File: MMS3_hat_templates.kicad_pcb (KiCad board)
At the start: 4 copper layers, 100 x 50 mm, 54 parts, among them J1 Chainbus in, J2 Chainbus Out, J3 Conn_01x04_Pin, J4 AMASS XT60 Male, J5 AMASS XT60 Female, J8 Conn_01x03_Pin, SW1 SW_DIP_x04, U1 SN74CB3Q3384APW, U2 M24C64, U4 AMS1117, U5 LM2596HVS-ADJRG

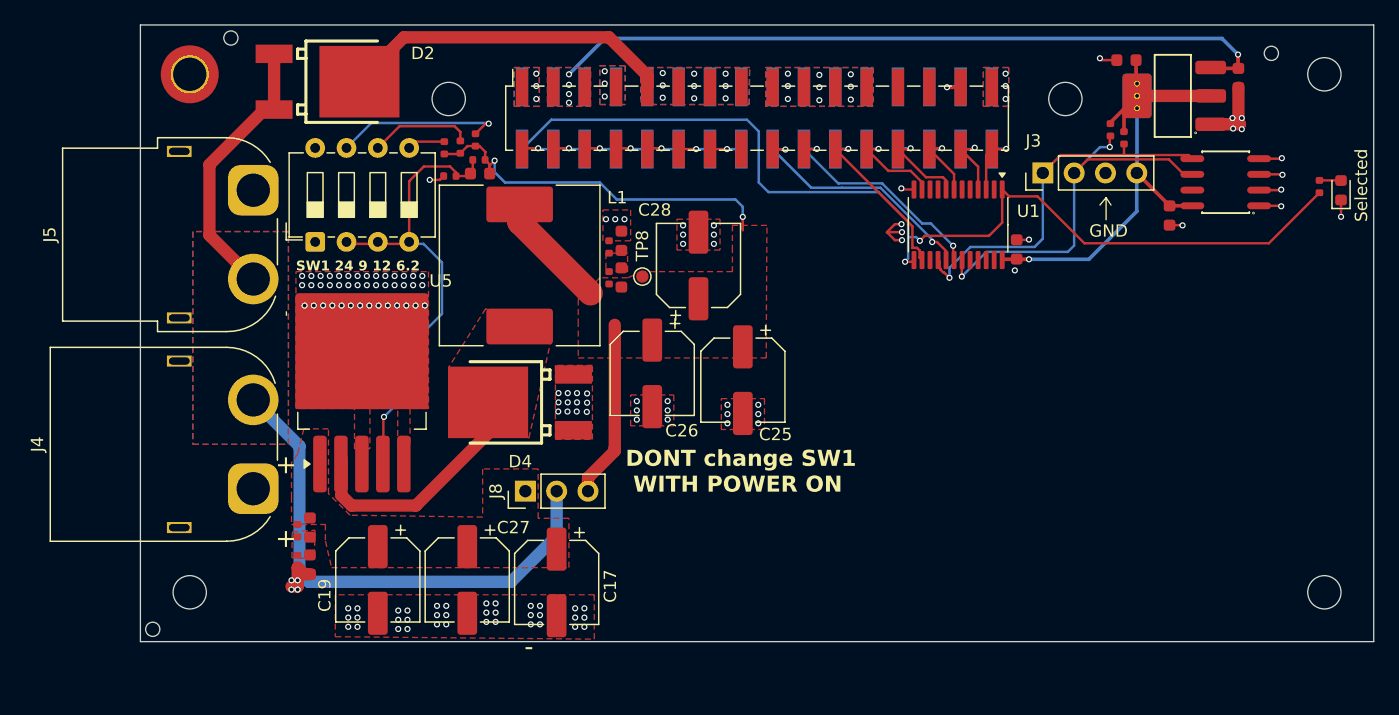
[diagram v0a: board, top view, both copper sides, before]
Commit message: template board cleansed
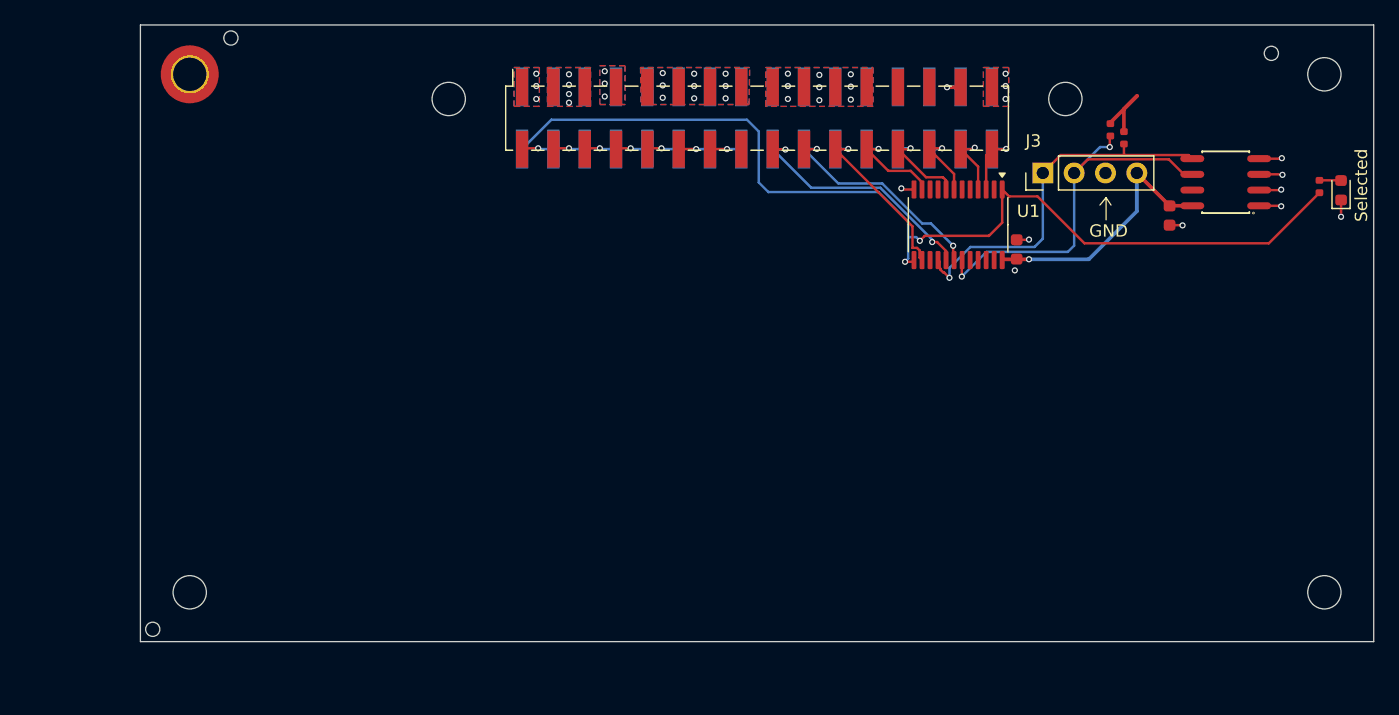
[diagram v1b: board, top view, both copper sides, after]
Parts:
- removed C16, C18: 10uF, PCM_JLCPCB:C_0603
- removed C17, C19, C25, C26, C27, C28: 47u, Capacitor_SMD:CP_Elec_6.3x7.7
- removed C20, C21, C23, C24: 100nF, PCM_JLCPCB:C_0603
- removed C22: 3.3nF, PCM_JLCPCB:C_0603
- removed D2, D4: MBRD10100CTTR, SMC_MBRD10100CTTR:TO-252-3_L6.5-W5.8-P4.58-TL
- removed J4: AMASS XT60 Male, XT60:AMASS_XT60PW-M_1x02_P7.20mm_Horizontal
- removed J5: AMASS XT60 Female, XT60:AMASS_XT60PW-F_1x02_P7.20mm_Horizontal
- removed J8: Conn_01x03_Pin, Connector_PinHeader_2.54mm:PinHeader_1x03_P2.54mm_Vertical
- removed L1: 100uH 4A, Inductor_SMD:L_Sunlord_SWRB1207S
- removed R10, R11, R17, R18: 33kΩ, PCM_JLCPCB:R_0402
- removed R12: 1kΩ, PCM_JLCPCB:R_0402
- removed R13: 18.7k, PCM_JLCPCB:R_0402
- removed R14: 16.5k, PCM_JLCPCB:R_0402
- removed R15: 9.53k, PCM_JLCPCB:R_0402
- removed R16: 5.11k, PCM_JLCPCB:R_0402
- removed SW1: SW_DIP_x04, Button_Switch_THT:SW_DIP_SPSTx04_Slide_6.7x11.72mm_W7.62mm_P2.54mm_LowProfile
- removed TP8: TestPoint, TestPoint:TestPoint_Pad_D1.0mm
- removed U4: AMS1117, PCM_JLCPCB:SOT-223-3_L6.5-W3.4-P2.30-LS7.0-BR
- removed U5: LM2596HVS-ADJRG, Package_TO_SOT_SMD:TO-263-5_TabPin3
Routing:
- net Vin: track 64.3 -> 0.00 mm
- net +5V: track 59.4 -> 0.00 mm, vias 5 -> 4
- net U_reg: track 55.0 -> 0.00 mm, vias 2 -> 0
- net Net-(U5-FB): track 38.3 -> 0.00 mm, vias 1 -> 0
- net BRD_VIN: track 27.1 -> 0.93 mm
- net Net-(D4-K): track 21.4 -> 0.00 mm
- net GND: track 27.6 -> 12.1 mm, vias 151 -> 27
- net Net-(R14-Pad1): track 13.8 -> 0.00 mm, vias 1 -> 0
- net +3V3: track 40.9 -> 27.7 mm
- net Net-(R15-Pad1): track 8.34 -> 0.00 mm
- net Net-(R16-Pad1): track 3.06 -> 0.00 mm
- removed copper zone on In1.Cu, net GND
- removed copper zone on In2.Cu, net GND
- removed copper zone on F.Cu, net Net-(C20-Pad2)
- removed copper zone on F.Cu, net Net-(C23-Pad2)
- removed copper zone on F.Cu, net Net-(D4-K)
- removed copper zone on F.Cu, net Net-(J8-Pin_1)
- removed copper zone on F.Cu, net U_reg
- removed copper zone on B.Cu, net Vin
- removed copper zone on F.Cu, net Vin
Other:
- copper layers 4 -> 2
- board text removed: "DONT change SW1 WITH POWER ON"
- board text removed: "SW1 24 9 12 6.2"

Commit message: done ( v 1.0 - check required )
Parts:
- removed H7, H8, H9: ~, PCM_JLCPCB:Hole_Tooling_JLCPCB
- added C10: 100n, PCM_JLCPCB:C_0603, F.Cu at (150.0, 127.0)
- added C11: 100n, PCM_JLCPCB:C_0603, F.Cu at (159.5, 127.0)
- added C12: 100n, PCM_JLCPCB:C_0603, F.Cu at (169.0, 127.0)
- added C13: 10u, Capacitor_SMD:CP_Elec_3x5.4, F.Cu at (106.0, 105.5)
- added C14: 10u, Capacitor_SMD:CP_Elec_3x5.4, F.Cu at (120.5, 112.0)
- added C15: 10u, Capacitor_SMD:CP_Elec_3x5.4, F.Cu at (106.0, 112.0)
- added C3: 100n, PCM_JLCPCB:C_0603, F.Cu at (133.0, 113.0)
- added C4: 100n, PCM_JLCPCB:C_0603, F.Cu at (93.0, 127.0)
- added C5: 100n, PCM_JLCPCB:C_0603, F.Cu at (102.5, 127.0)
- added C6: 100n, PCM_JLCPCB:C_0603, F.Cu at (112.0, 127.0)
- added C7: 100n, PCM_JLCPCB:C_0603, F.Cu at (121.5, 127.0)
- added C8: 100n, PCM_JLCPCB:C_0603, F.Cu at (131.0, 127.0)
- added C9: 100n, PCM_JLCPCB:C_0603, F.Cu at (140.5, 127.0)
- added J10: Conn_01x02_Socket, Connector_JST:JST_XH_S2B-XH-A_1x02_P2.50mm_Horizontal, F.Cu at (145.8, 132.6)
- added J11: Conn_01x02_Socket, Connector_JST:JST_XH_S2B-XH-A_1x02_P2.50mm_Horizontal, F.Cu at (155.2, 132.6)
- added J12: Conn_01x02_Socket, Connector_JST:JST_XH_S2B-XH-A_1x02_P2.50mm_Horizontal, F.Cu at (164.8, 132.6)
- added J4: Conn_01x02_Socket, Connector_JST:JST_XH_S2B-XH-A_1x02_P2.50mm_Horizontal, F.Cu at (88.8, 132.6)
- added J5: Conn_01x02_Socket, Connector_JST:JST_XH_S2B-XH-A_1x02_P2.50mm_Horizontal, F.Cu at (98.2, 132.6)
- added J6: Conn_01x02_Socket, Connector_JST:JST_XH_S2B-XH-A_1x02_P2.50mm_Horizontal, F.Cu at (107.8, 132.6)
- added J7: Conn_01x02_Socket, Connector_JST:JST_XH_S2B-XH-A_1x02_P2.50mm_Horizontal, F.Cu at (117.2, 132.6)
- added J8: Conn_01x02_Socket, Connector_JST:JST_XH_S2B-XH-A_1x02_P2.50mm_Horizontal, F.Cu at (126.8, 132.6)
- added J9: Conn_01x02_Socket, Connector_JST:JST_XH_S2B-XH-A_1x02_P2.50mm_Horizontal, F.Cu at (136.2, 132.6)
- added U10: MAX31855KASA, Package_SO:SOIC-8_3.9x4.9mm_P1.27mm, F.Cu at (145.5, 122.5)
- added U11: MAX31855KASA, Package_SO:SOIC-8_3.9x4.9mm_P1.27mm, F.Cu at (155.0, 122.5)
- added U12: MAX31855KASA, Package_SO:SOIC-8_3.9x4.9mm_P1.27mm, F.Cu at (164.5, 122.5)
- added U14: AZ1117H-3.3TRE1, Package_TO_SOT_SMD:SOT-223-3_TabPin2, F.Cu at (113.0, 109.0)
- added U3: TCA9535PWR, Package_SO:TSSOP-24_4.4x7.8mm_P0.65mm, F.Cu at (133.0, 107.5)
- added U4: MAX31855KASA, Package_SO:SOIC-8_3.9x4.9mm_P1.27mm, F.Cu at (88.5, 122.5)
- added U5: MAX31855KASA, Package_SO:SOIC-8_3.9x4.9mm_P1.27mm, F.Cu at (98.0, 122.5)
- added U6: MAX31855KASA, Package_SO:SOIC-8_3.9x4.9mm_P1.27mm, F.Cu at (107.5, 122.5)
- added U7: MAX31855KASA, Package_SO:SOIC-8_3.9x4.9mm_P1.27mm, F.Cu at (117.0, 122.5)
- added U8: MAX31855KASA, Package_SO:SOIC-8_3.9x4.9mm_P1.27mm, F.Cu at (126.5, 122.5)
- added U9: MAX31855KASA, Package_SO:SOIC-8_3.9x4.9mm_P1.27mm, F.Cu at (136.0, 122.5)
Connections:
- net /Bus_switch/Chainbus.CS renamed /ChainBus.CS
- net /Bus_switch/Chainbus.MOSI renamed /ChainBus.MOSI
- U1 pad 10: /Bus_switch/Chainbus.SCK -> /ChainBus.SCK
- U1 pad 6: /Bus_switch/Chainbus.MISO -> /ChainBus.MISO
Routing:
- net +3V3: track 27.7 -> 174.3 mm, vias 1 -> 11
- net /ChainBus.MISO: track 0.00 -> 135.6 mm, vias 0 -> 2
- net /ChainBus.SCK: track 0.00 -> 115.2 mm, vias 0 -> 2
- net /GPIO_0: track 0.00 -> 52.9 mm, vias 0 -> 2
- net /GPIO_1: track 0.00 -> 42.9 mm, vias 0 -> 2
- net /GPIO_7: track 0.00 -> 37.4 mm, vias 0 -> 4
- net /GPIO_8: track 0.00 -> 35.3 mm, vias 0 -> 2
- net /GPIO_2: track 0.00 -> 32.5 mm, vias 0 -> 2
- net /GPIO_6: track 0.00 -> 30.4 mm, vias 0 -> 4
- net /GPIO_5: track 0.00 -> 22.0 mm, vias 0 -> 2
- net +5V: track 0.00 -> 20.1 mm
- net /GPIO_3: track 0.00 -> 19.5 mm, vias 0 -> 2
- net /GPIO_4: track 0.00 -> 15.6 mm, vias 0 -> 2
- net /Bus_switch/Chainbus.SCL: track 32.6 -> 43.2 mm
- net /Bus_switch/Chainbus.SDA: track 30.3 -> 39.7 mm
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
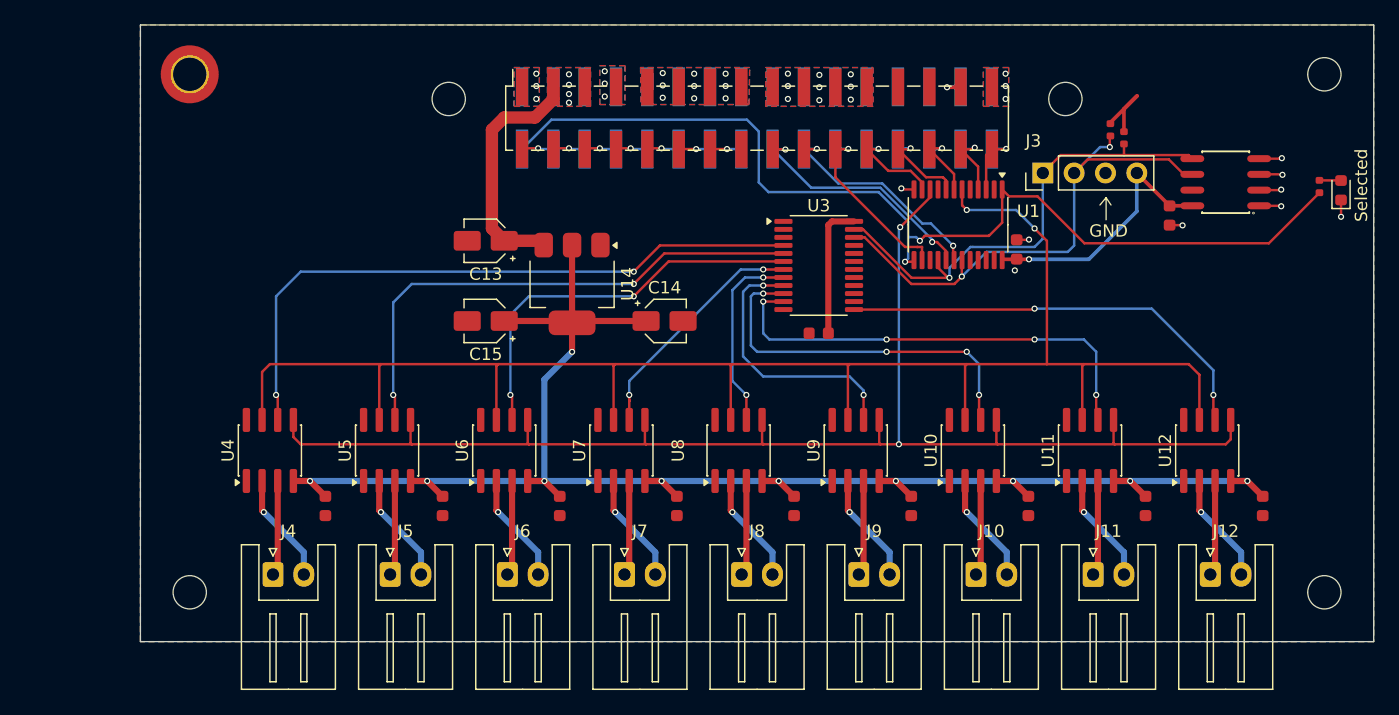
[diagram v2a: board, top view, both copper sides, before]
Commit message: fixed selected led polarity
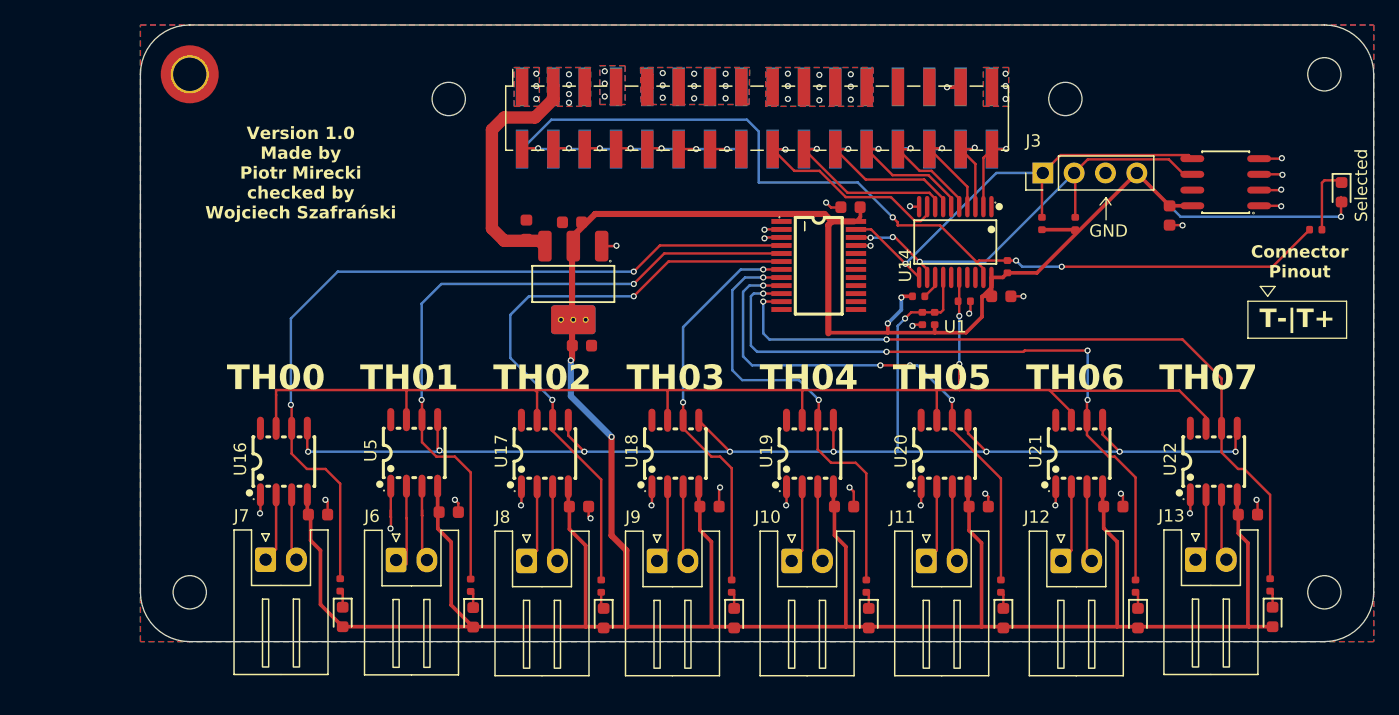
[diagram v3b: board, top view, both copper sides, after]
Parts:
- removed C13, C14, C15: 10u, Capacitor_SMD:CP_Elec_3x5.4
- removed C3: 100n, PCM_JLCPCB:C_0603
- removed D1: LED, LED_SMD:LED_0603_1608Metric
- removed J4, J5: Conn_01x02_Socket, Connector_JST:JST_XH_S2B-XH-A_1x02_P2.50mm_Horizontal
- removed PN1: ~, PCM_JLCPCB:Part_Num_JLCPCB
- removed U10, U11, U12, U4, U6, U7, U8, U9: MAX31855KASA, Package_SO:SOIC-8_3.9x4.9mm_P1.27mm
- removed U3: TCA9535PWR, Package_SO:TSSOP-24_4.4x7.8mm_P0.65mm
- added C16: 10uF, PCM_JLCPCB:C_0603, F.Cu at (109.3, 104.6)
- added C17: 10uF, PCM_JLCPCB:C_0603, F.Cu at (113.0, 104.0)
- added C18: 10uF, PCM_JLCPCB:C_0603, F.Cu at (113.8, 114.0)
- added D11: Red, PCM_JLCPCB:D_0603, F.Cu at (105.0, 136.0)
- added D12: Red, PCM_JLCPCB:D_0603, F.Cu at (94.4, 136.0)
- added D13: Red, PCM_JLCPCB:D_0603, F.Cu at (115.6, 136.1)
- added D14: Red, PCM_JLCPCB:D_0603, F.Cu at (126.1, 136.1)
- added D15: Red, PCM_JLCPCB:D_0603, F.Cu at (137.1, 136.1)
- added D16: Red, PCM_JLCPCB:D_0603, F.Cu at (148.0, 136.1)
- added D17: Red, PCM_JLCPCB:D_0603, F.Cu at (158.9, 136.1)
- added D18: Red, PCM_JLCPCB:D_0603, F.Cu at (169.8, 136.0)
- added D20: Red, PCM_JLCPCB:D_0603, F.Cu at (175.4, 101.6)
- added J13: Conn_01x02_Socket, Connector_JST:JST_XH_S2B-XH-A_1x02_P2.50mm_Horizontal, F.Cu at (163.6, 131.4)
- added R10: 330Ω, PCM_JLCPCB:R_0402, F.Cu at (104.8, 133.4)
- added R11: 330Ω, PCM_JLCPCB:R_0402, F.Cu at (94.2, 133.4)
- added R12: 330Ω, PCM_JLCPCB:R_0402, F.Cu at (115.4, 133.5)
- added R13: 330Ω, PCM_JLCPCB:R_0402, F.Cu at (125.9, 133.5)
- added R14: 330Ω, PCM_JLCPCB:R_0402, F.Cu at (136.9, 133.5)
- added R15: 330Ω, PCM_JLCPCB:R_0402, F.Cu at (147.8, 133.5)
- added R16: 330Ω, PCM_JLCPCB:R_0402, F.Cu at (158.7, 133.5)
- added R17: 330Ω, PCM_JLCPCB:R_0402, F.Cu at (169.6, 133.4)
- added R20: 330Ω, PCM_JLCPCB:R_0402, F.Cu at (173.3, 104.6)
- added R4: 10kΩ, PCM_JLCPCB:R_0402, F.Cu at (141.4, 111.8)
- added R5: 10kΩ, PCM_JLCPCB:R_0402, F.Cu at (153.8, 104.1)
- added R8: 10kΩ, PCM_JLCPCB:R_0402, F.Cu at (144.8, 110.4)
- added R9: 10kΩ, PCM_JLCPCB:R_0402, F.Cu at (151.1, 104.1)
- added U13: AMS1117, PCM_JLCPCB:SOT-223-3_L6.5-W3.4-P2.30-LS7.0-BR, F.Cu at (113.1, 108.9)
- added U16: MAX31855KASA+T, MAX31855KASA:SO-8_L4.9-W3.9-P1.27-LS5.9-BL, F.Cu at (89.6, 123.4)
- added U17: MAX31855KASA+T, MAX31855KASA:SO-8_L4.9-W3.9-P1.27-LS5.9-BL, F.Cu at (110.8, 122.8)
- added U18: MAX31855KASA+T, MAX31855KASA:SO-8_L4.9-W3.9-P1.27-LS5.9-BL, F.Cu at (121.4, 122.8)
- added U19: MAX31855KASA+T, MAX31855KASA:SO-8_L4.9-W3.9-P1.27-LS5.9-BL, F.Cu at (132.3, 122.8)
- added U20: MAX31855KASA+T, MAX31855KASA:SO-8_L4.9-W3.9-P1.27-LS5.9-BL, F.Cu at (143.2, 122.8)
- added U21: MAX31855KASA+T, MAX31855KASA:SO-8_L4.9-W3.9-P1.27-LS5.9-BL, F.Cu at (154.1, 122.8)
- added U22: MAX31855KASA+T, MAX31855KASA:SO-8_L4.9-W3.9-P1.27-LS5.9-BL, F.Cu at (165.0, 123.4)
- C10, C11, C12, C4, C5, C6, C7, C8, C9: value 100n -> 100nF
- R1: value 330Ω -> 10kΩ
- U1: value SN74CB3Q3384APW -> SN74CB3Q3245PWR; footprint Package_SO:TSSOP-24_4.4x7.8mm_P0.65mm -> SN74CB3Q3245PWR:TSSOP-20_L6.5-W4.4-P0.65-LS6.4-BL
- U14: value AZ1117H-3.3TRE1 -> TCA9535PWR_C130204; footprint Package_TO_SOT_SMD:SOT-223-3_TabPin2 -> TCA9535PWR:TSSOP-24_L7.8-W4.4-P0.65-LS6.4-BL
- U5: value MAX31855KASA -> MAX31855KASA+T; footprint Package_SO:SOIC-8_3.9x4.9mm_P1.27mm -> MAX31855KASA:SO-8_L4.9-W3.9-P1.27-LS5.9-BL
- moved C12 41.3 mm to (135.6, 102.8), turned to 180 degrees
- moved J7 29.1 mm to (88.2, 131.4)
- moved R1 26.1 mm to (148.3, 107.6), turned to -90 degrees
- moved R3 21.2 mm to (142.4, 111.8), turned to 90 degrees
- moved R2 20.6 mm to (141.1, 110.0), turned to 0 degrees
- moved U14 20.1 mm to (133.0, 107.5)
- moved J8 17.5 mm to (109.3, 131.5)
- moved J9 16.4 mm to (119.9, 131.5)
- moved J10 15.0 mm to (130.8, 131.5)
- moved J11 13.6 mm to (141.7, 131.5)
- moved J12 12.2 mm to (152.6, 131.5)
- moved C5 10.1 mm to (92.4, 127.7), turned to 0 degrees
- moved C4 10.0 mm to (103.0, 127.5), turned to 0 degrees
- moved J6 9.09 mm to (98.7, 131.4)
- moved C11 8.33 mm to (167.8, 127.7), turned to 0 degrees
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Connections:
- J10 pad 1: Net-(J10-Pin_1) -> /Thermocouple4/T-
- J10 pad 2: Net-(J10-Pin_2) -> /Thermocouple4/T+
- J11 pad 1: Net-(J11-Pin_1) -> /Thermocouple5/T-
- J11 pad 2: Net-(J11-Pin_2) -> /Thermocouple5/T+
- J12 pad 1: Net-(J12-Pin_1) -> /Thermocouple6/T-
- J12 pad 2: Net-(J12-Pin_2) -> /Thermocouple6/T+
- J6 pad 1: Net-(J6-Pin_1) -> /Thermocouple1/T-
- J6 pad 2: Net-(J6-Pin_2) -> /Thermocouple1/T+
- J7 pad 1: Net-(J7-Pin_1) -> /Thermocouple/T-
- J7 pad 2: Net-(J7-Pin_2) -> /Thermocouple/T+
- J8 pad 1: Net-(J8-Pin_1) -> /Thermocouple2/T-
- J8 pad 2: Net-(J8-Pin_2) -> /Thermocouple2/T+
- J9 pad 1: Net-(J9-Pin_1) -> /Thermocouple3/T-
- J9 pad 2: Net-(J9-Pin_2) -> /Thermocouple3/T+
- R1 pad 2: Net-(D1-A) -> +3V3
- R2 pad 2: /Bus_switch/Chainbus.SCL -> /ChainBus.CS
- R3 pad 2: /Bus_switch/Chainbus.SDA -> /ChainBus.SCK
- U1 pad 1: /Bus_switch/SEL1 -> unconnected-(U1-NC-Pad1)
- U1 pad 10: /ChainBus.SCK -> GND
- U1 pad 11: /Bus_switch/Chainbus_In.SCK -> /Bus_switch/Chainbus.SDA
- U1 pad 12: GND -> /Bus_switch/Chainbus.SCL
- U1 pad 13: /Bus_switch/SEL1 -> /ChainBus.CS
- U1 pad 14: /Bus_switch/Chainbus_In.CS -> /ChainBus.SCK
- U1 pad 15: /ChainBus.CS -> /ChainBus.MOSI
- U1 pad 16: /Bus_switch/Chainbus.SDA -> /ChainBus.MISO
- U1 pad 17: /Bus_switch/Chainbus_In.SDA -> /Bus_switch/Chainbus.TX
- U1 pad 18: /Bus_switch/Chainbus_In.SCL -> /Bus_switch/Chainbus.RX
- U1 pad 19: /Bus_switch/Chainbus.SCL -> /Bus_switch/SEL1
- U1 pad 2: /Bus_switch/Chainbus.RX -> /Bus_switch/Chainbus_In.RX
- U1 pad 20: unconnected-(U1-2B4-Pad20) -> +3V3
- U1 pad 3: /Bus_switch/Chainbus_In.RX -> /Bus_switch/Chainbus_In.TX
- U1 pad 4: /Bus_switch/Chainbus_In.TX -> /Bus_switch/Chainbus_In.MISO
- U1 pad 5: /Bus_switch/Chainbus.TX -> /Bus_switch/Chainbus_In.MOSI
- U1 pad 6: /ChainBus.MISO -> /Bus_switch/Chainbus_In.SCK
- U1 pad 7: /Bus_switch/Chainbus_In.MISO -> /Bus_switch/Chainbus_In.CS
- U1 pad 8: /Bus_switch/Chainbus_In.MOSI -> /Bus_switch/Chainbus_In.SCL
- U1 pad 9: /ChainBus.MOSI -> /Bus_switch/Chainbus_In.SDA
- U14 pad 1: GND -> unconnected-(U14-~{INT}-Pad1)
- U14 pad 2: +3V3 -> GND
- U14 pad 3: +5V -> GND
- U5 pad 2: Net-(J5-Pin_2) -> /Thermocouple1/T-
- U5 pad 3: Net-(J5-Pin_1) -> /Thermocouple1/T+
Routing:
- net +3V3: track 174.3 -> 305.2 mm, vias 11 -> 5
- net /GPIO_8: track 35.3 -> 0.00 mm, vias 2 -> 0
- net GND: track 12.1 -> 44.0 mm, vias 27 -> 48
- net /ChainBus.MISO: track 135.6 -> 105.0 mm
- net /GPIO_6: track 30.4 -> 54.8 mm
- net /GPIO_7: track 37.4 -> 61.1 mm, vias 4 -> 2
- net /GPIO_5: track 22.0 -> 43.4 mm, vias 2 -> 4
- net /GPIO_4: track 15.6 -> 36.5 mm
- net /GPIO_2: track 32.5 -> 48.5 mm
- net /GPIO_0: track 52.9 -> 66.0 mm
- net /GPIO_3: track 19.5 -> 32.6 mm
- net /GPIO_1: track 42.9 -> 55.9 mm
- net Net-(J8-Pin_2): track 8.98 -> 0.00 mm, vias 1 -> 0
- net Net-(J7-Pin_2): track 8.98 -> 0.00 mm, vias 1 -> 0
- net Net-(J6-Pin_2): track 8.98 -> 0.00 mm, vias 1 -> 0
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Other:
- outline, holes or cut-outs redrawn
- board text added: "3"
- board text added: "Connector Pinout"
- board text added: "Front and Back keepout zone for DIN rail mount"
- board text added: "T-|T+"
- board text added: "TH00"
- board text added: "TH01"
- board text added: "TH02"
- board text added: "TH03"
- board text added: "TH04"
- board text added: "TH05"
- board text added: "TH06"
- board text added: "TH07"
- board text added: "Version 1.0 Made by Piotr Mirecki checked by Wojciech Szafrański"
- board text removed: "2"
